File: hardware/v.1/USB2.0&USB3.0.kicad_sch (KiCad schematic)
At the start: 21 parts, among them J5 USB_A_Stacked, J78 USB3_A, J80 USB3_A, U3 ULC0524P, U4 ULC0524P, U5 ULC0524P

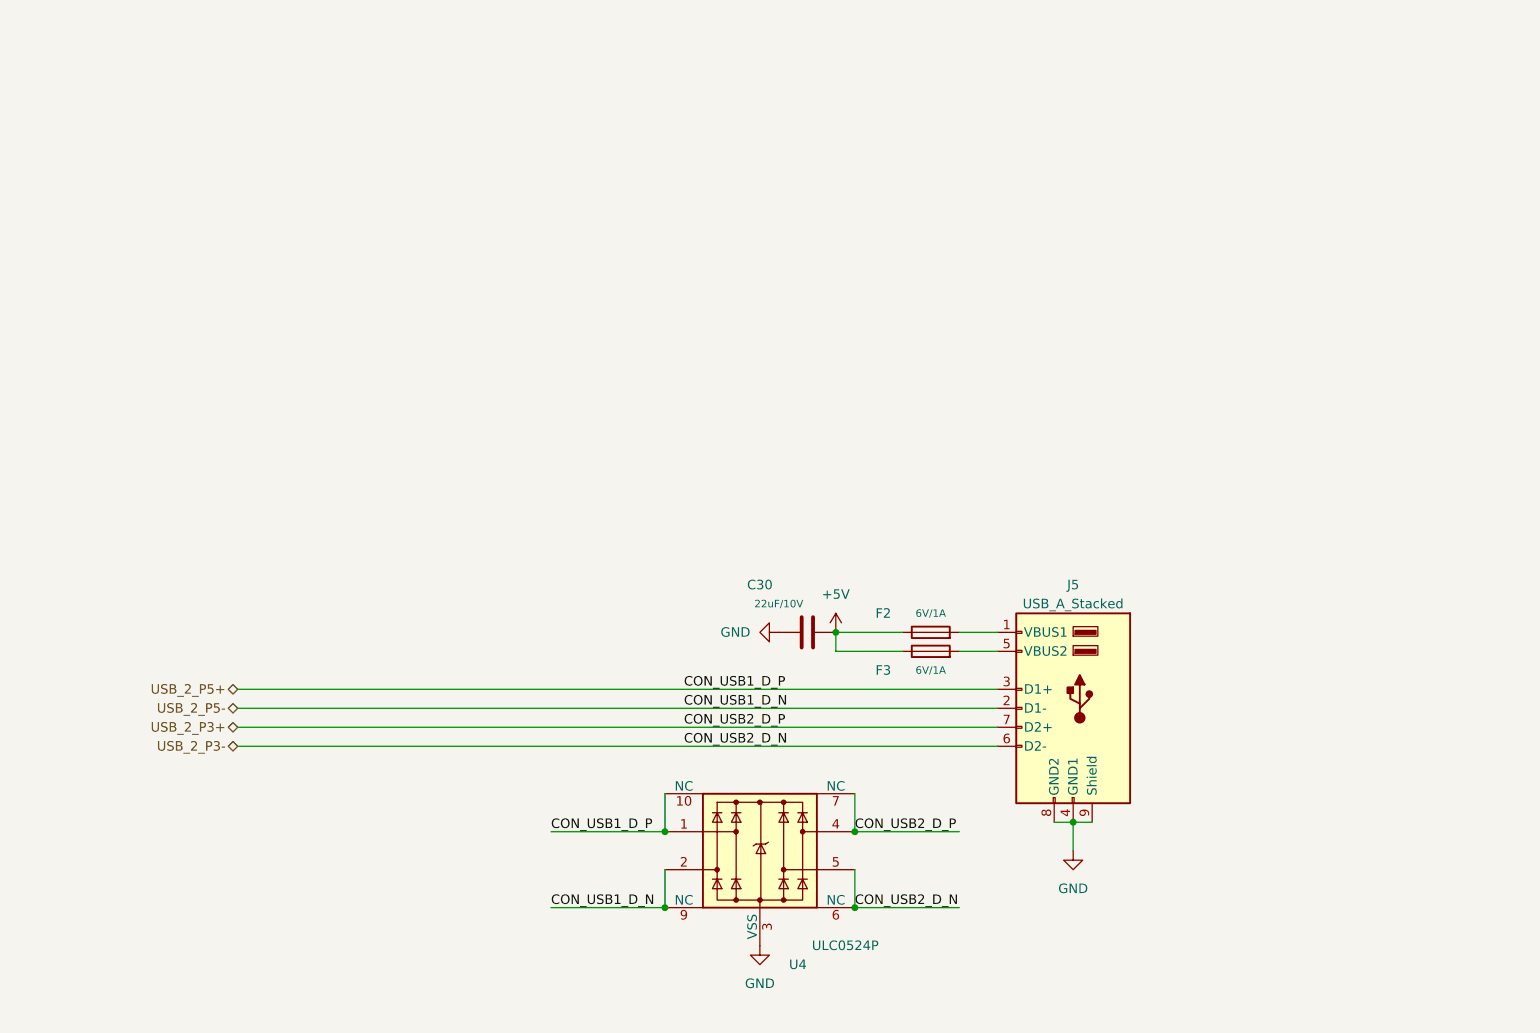
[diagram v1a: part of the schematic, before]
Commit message: wire up the 3 pcie lanes coming from the realtek ic and add 2 usbc ports
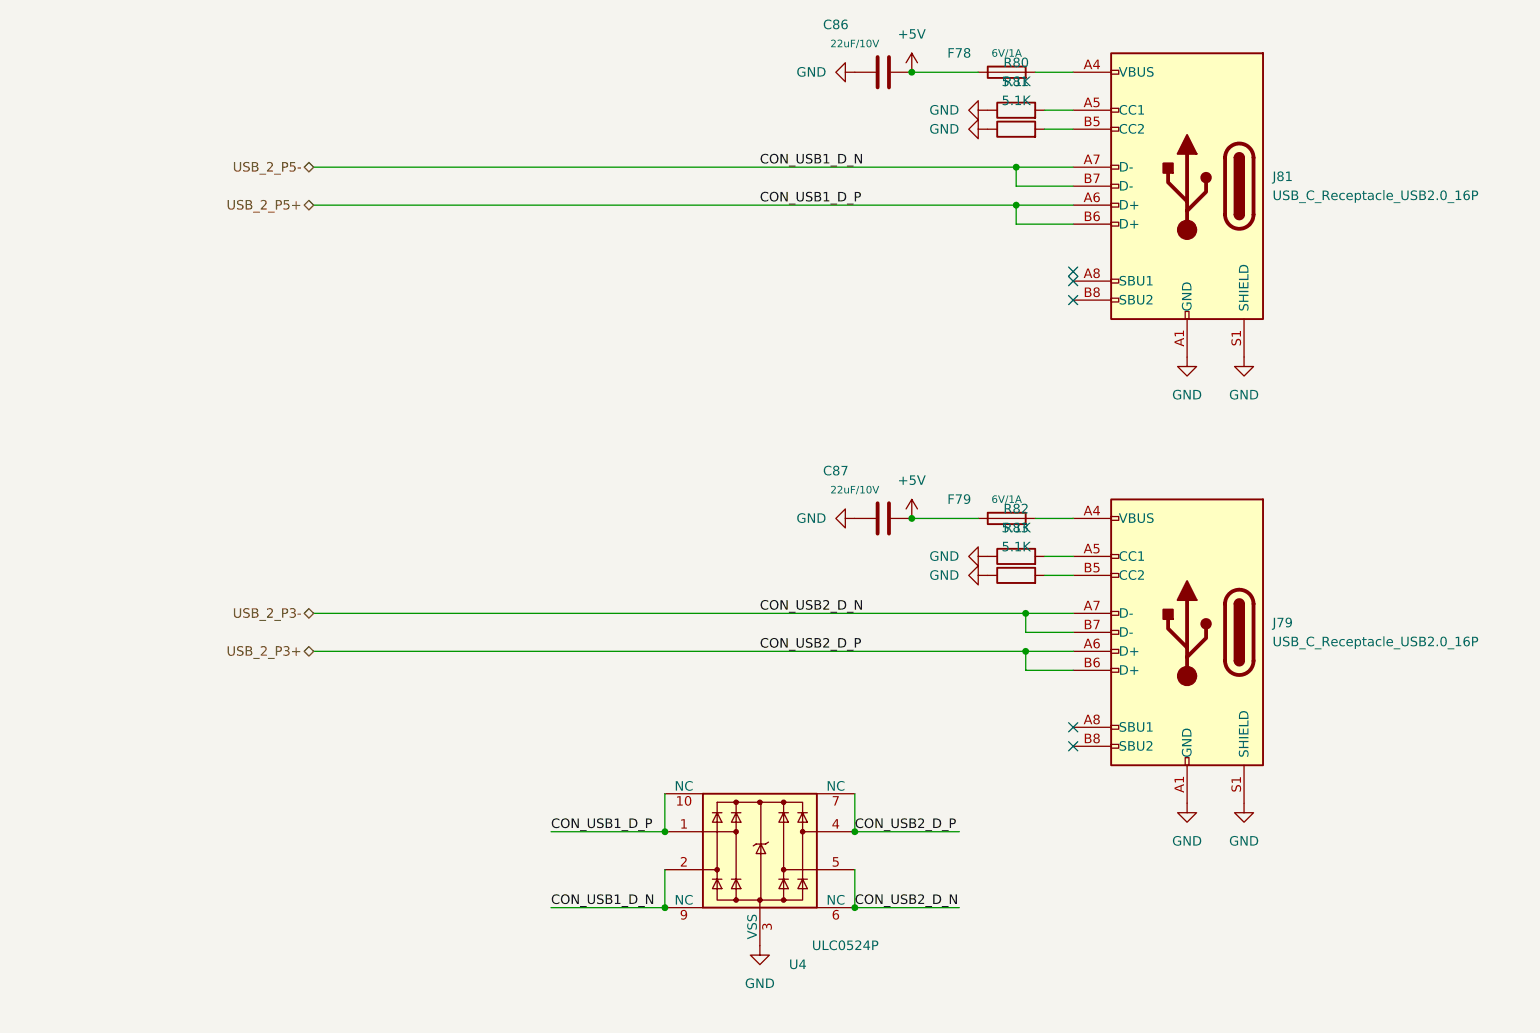
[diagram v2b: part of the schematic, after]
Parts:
- removed C30: 22uF/10V, A_HDJ_Library:C_0603_1608Metric, symbol Device:C
- removed F2, F3: 6V/1A, A_HDJ_Library:Fuse_0805_2012Metric, symbol Device:Fuse
- removed J5: USB_A_Stacked, A_HDJ_Library:USB_A_CUI_UJ2-ADH-TH_Horizontal_Stacked, symbol Connector:USB_A_Stacked
- added C86, C87: 22uF/10V, A_HDJ_Library:C_0603_1608Metric, symbol Device:C
- added F78, F79: 6V/1A, A_HDJ_Library:Fuse_0805_2012Metric, symbol Device:Fuse
- added J79, J81: USB_C_Receptacle_USB2.0_16P, A_HDJ_Library:USB_C_Receptacle_G-Switch_GT-USB-7010ASV, symbol Connector:USB_C_Receptacle_USB2.0_16P
- added R80, R81, R82, R83: 5.1K, A_HDJ_Library:R_0402_1005Metric, symbol Device:R
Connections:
- net +5V: now also C86.2, C87.2, F78.1, F79.1
- net GND: now also C86.1, C87.1, J79.A1 (GND), J79.A12 (GND), J79.B1 (GND), J79.B12 (GND), J79.S1 (SHIELD), J81.A1 (GND), J81.A12 (GND), J81.B1 (GND), J81.B12 (GND), J81.S1 (SHIELD), R80.1, R81.1, R82.1, R83.1
- net USB_2_P3+: now also J79.A6 (D+), J79.B6 (D+)
- net USB_2_P3-: now also J79.A7 (D-), J79.B7 (D-)
- net USB_2_P5+: now also J81.A6 (D+), J81.B6 (D+)
- net USB_2_P5-: now also J81.A7 (D-), J81.B7 (D-)
- new net: F78.2, J81.A4 (VBUS), J81.A9 (VBUS), J81.B4 (VBUS), J81.B9 (VBUS)
- new net: J81.A5 (CC1), R80.2
- new net: J81.B5 (CC2), R81.2
- new net: F79.2, J79.A4 (VBUS), J79.A9 (VBUS), J79.B4 (VBUS), J79.B9 (VBUS)
- new net: J79.A5 (CC1), R82.2
- new net: J79.B5 (CC2), R83.2
- no-connect marks 0 -> 5

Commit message: pretty much finish the board, did bios chip, gpio, 4x sata
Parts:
- added C88, C89: 22uF/10V, A_HDJ_Library:C_0603_1608Metric, symbol Device:C
- added F80, F81: 6V/1A, A_HDJ_Library:Fuse_0805_2012Metric, symbol Device:Fuse
- added J82, J83: USB_A, Connector_USB:USB_A_Receptacle_GCT_USB1046, symbol Connector:USB_A
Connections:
- net +5V: now also C88.2, C89.2, F80.1, F81.1
- net GND: now also C88.1, C89.1, J82.4 (GND), J82.5 (Shield), J83.4 (GND), J83.5 (Shield)
- net USB_2_P3+: now also U4.5, U4.6 (NC); no longer U4.4, U4.7 (NC)
- net USB_2_P3-: now also U4.4, U4.7 (NC); no longer U4.5, U4.6 (NC)
- net USB_2_P5+: now also U4.2, U4.9 (NC); no longer U4.1, U4.10 (NC)
- net USB_2_P5-: now also U4.1, U4.10 (NC); no longer U4.2, U4.9 (NC)
- new net: F81.2, J83.1 (VBUS)
- new net: F80.2, J82.1 (VBUS)
- new net USB_2_P4+: J82.3 (D+)
- new net USB_2_P4-: J82.2 (D-)
- new net USB_2_P8+: J83.3 (D+)
- new net USB_2_P8-: J83.2 (D-)

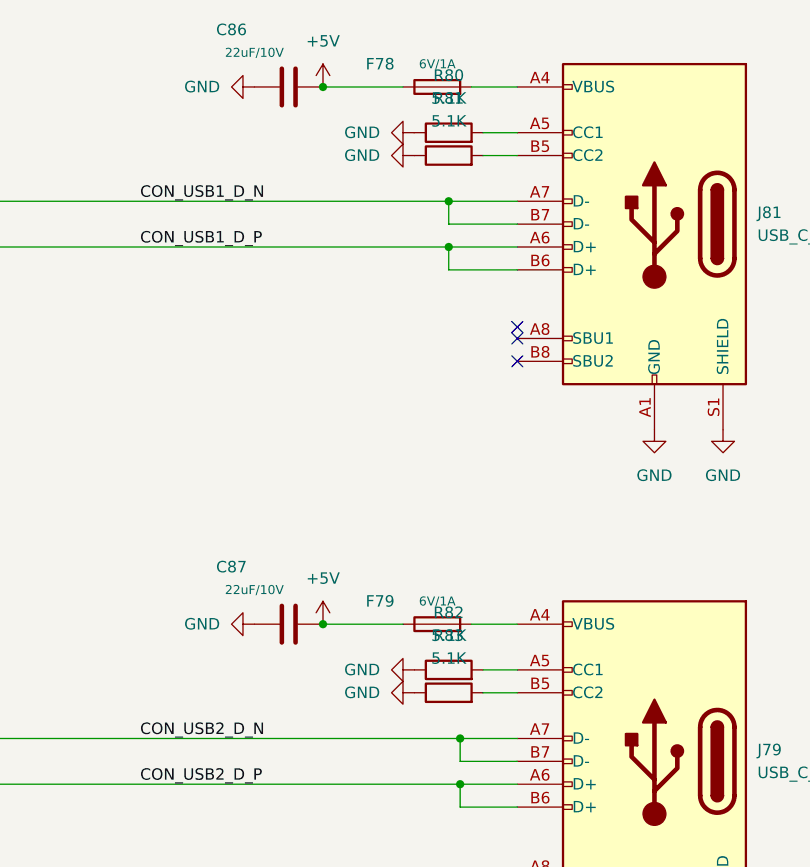
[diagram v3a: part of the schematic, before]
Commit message: thicken the power traces, make 3v3 and 5v beefier and fix usb c
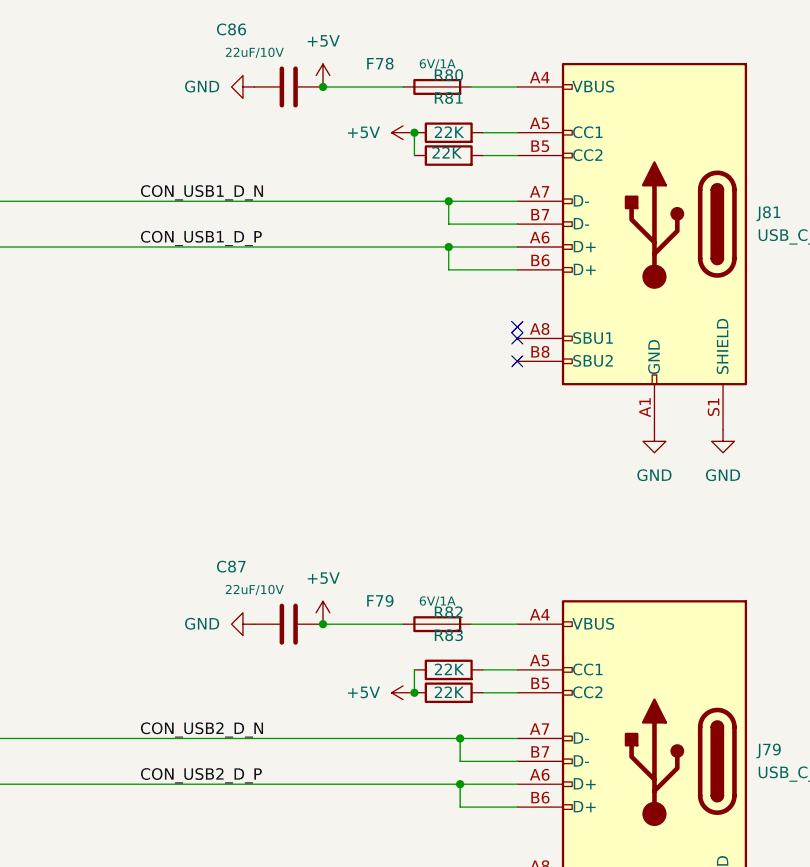
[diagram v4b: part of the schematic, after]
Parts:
- R80, R81, R82, R83: value 5.1K -> 22K
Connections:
- net +5V: now also R80.1, R81.1, R82.1, R83.1
- net GND: no longer R80.1, R81.1, R82.1, R83.1

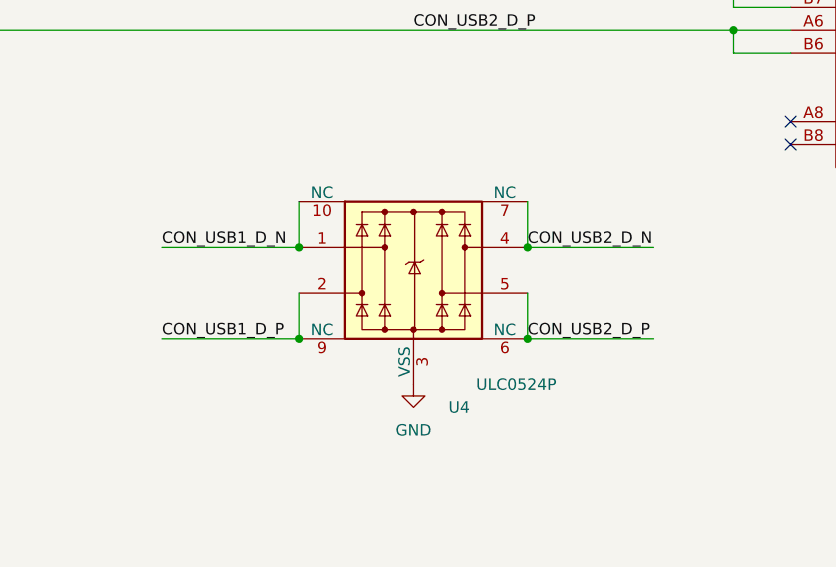
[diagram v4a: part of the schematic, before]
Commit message: remove some footprints to use digikey ones
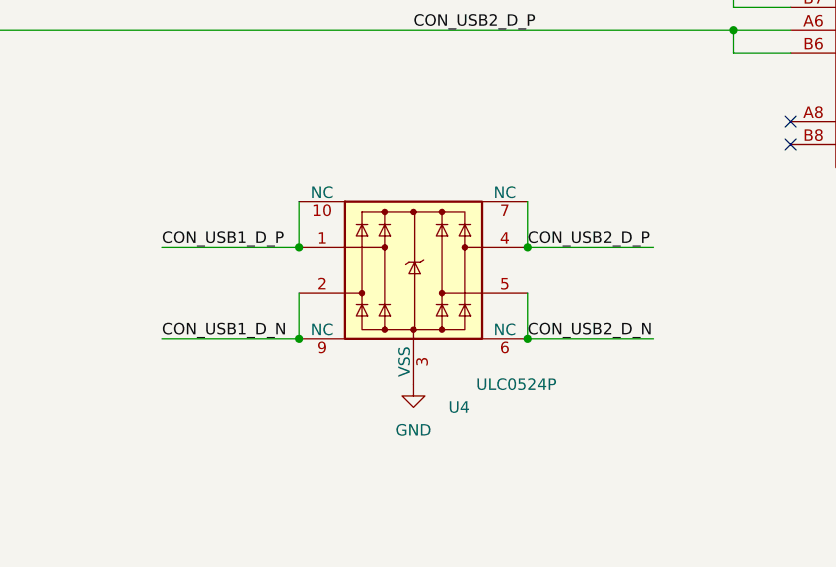
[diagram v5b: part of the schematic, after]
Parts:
- J79, J81: footprint A_HDJ_Library:USB_C_Receptacle_G-Switch_GT-USB-7010ASV -> Connector_USB:USB_C_Receptacle_JAE_DX07S016JA1R1500
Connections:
- net USB_2_P3+: now also U4.4, U4.7 (NC); no longer U4.5, U4.6 (NC)
- net USB_2_P3-: now also U4.5, U4.6 (NC); no longer U4.4, U4.7 (NC)
- net USB_2_P5+: now also U4.1, U4.10 (NC); no longer U4.2, U4.9 (NC)
- net USB_2_P5-: now also U4.2, U4.9 (NC); no longer U4.1, U4.10 (NC)
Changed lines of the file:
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@@
 		)
 	)
-	(label "CON_USB2_D_P"
+	(label "CON_USB2_D_N"
 		(at 299.72 137.16 0)
 		(effects
@@
 		)
 	)
-	(label "CON_USB1_D_N"
+	(label "CON_USB1_D_P"
 		(at 259.08 127 0)
 		(effects
@@
 		)
 	)
-	(label "CON_USB2_D_N"
+	(label "CON_USB2_D_P"
 		(at 299.72 127 0)
 		(effects
@@
 		)
 	)
-	(label "CON_USB1_D_P"
+	(label "CON_USB1_D_N"
 		(at 259.08 137.16 0)
 		(effects
@@
 			)
 		)
-		(property "Footprint" "A_HDJ_Library:USB_C_Receptacle_G-Switch_GT-USB-7010ASV"
+		(property "Footprint" "Connector_USB:USB_C_Receptacle_JAE_DX07S016JA1R1500"
 			(at 340.36 40.64 0)
 			(effects
@@
 			)
 		)
-		(property "Footprint" "A_HDJ_Library:USB_C_Receptacle_G-Switch_GT-USB-7010ASV"
+		(property "Footprint" "Connector_USB:USB_C_Receptacle_JAE_DX07S016JA1R1500"
 			(at 340.36 100.33 0)
 			(effects
